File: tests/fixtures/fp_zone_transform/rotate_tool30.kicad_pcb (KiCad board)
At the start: 2 copper layers, 45 x 40 mm, 1 part

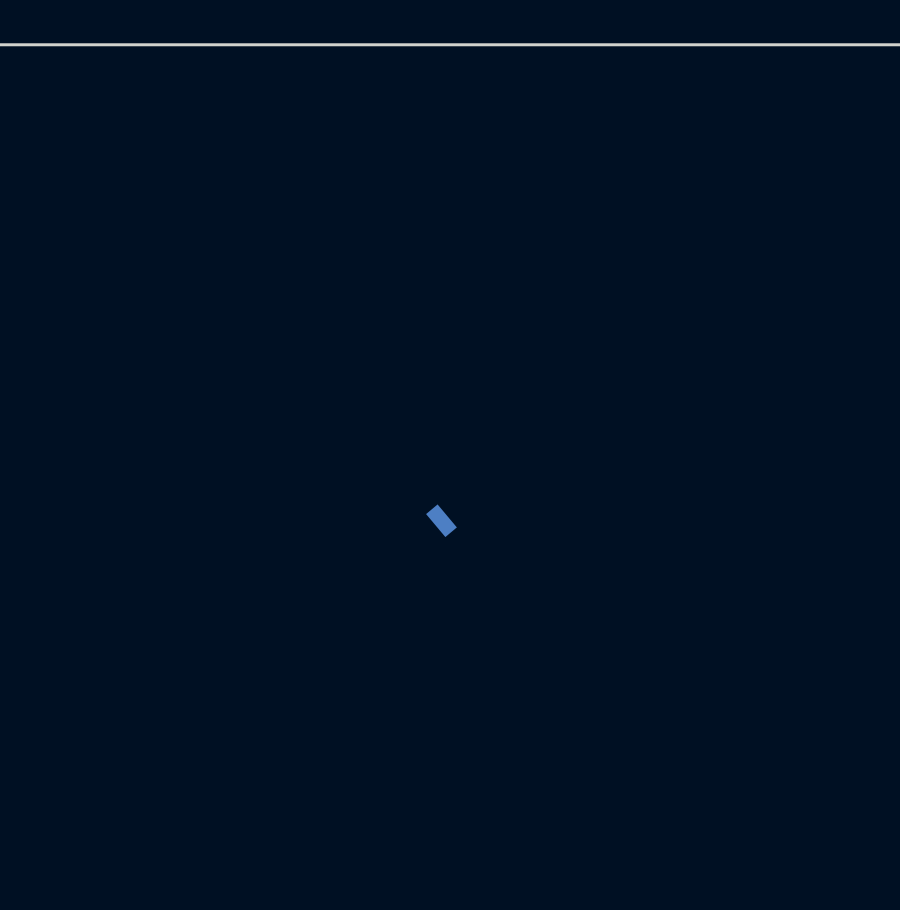
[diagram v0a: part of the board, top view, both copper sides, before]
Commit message: fix(pcb): turn footprint text angles with their footprint (#6126)
KiCad stores property/fp_text (at x y ANGLE) angles board-absolute, like
pad angles, so rotating or flipping a footprint must rewrite them. Pinned
against pcbnew 10.0.1 goldens (tests/fixtures/fp_zone_transform/, now
carrying keep-upright and unlocked user texts plus Rotate() cases):

- Footprint.__setattr__ maps text angles from the old placement frame to
  the new one (SetOrientation semantics: +delta on the same side, a -> -a
  under the left/right side swap), for both the S-expression nodes and the
  parsed FootprintText objects. This covers update_footprint_position,
  placement writeback, pcb move-footprint and snap-rotation.
- Footprint.keep_texts_upright / keep_footprint_texts_upright apply
  KiCad's FOOTPRINT::Rotate keep-upright step (>= 180 turns by -180 and
  swaps justification; (unlocked yes) / legacy `unlocked` texts are left
  alone). Used by pcb modify rotate, the recovery rotate strategy and the
  mirror strategy (pcb modify flip), replacing its `180 - a` text angle,
  which was 180 degrees off for unlocked and some keep-upright text.
- transform_footprint_text_nodes is the raw-node counterpart of
  transform_footprint_zone_nodes, used by pcb modify rotate.
- snap-rotation now turns pad angles by the snap amount.

Co-Authored-By: Claude Opus 5.5 (1M context) <noreply@anthropic.com>
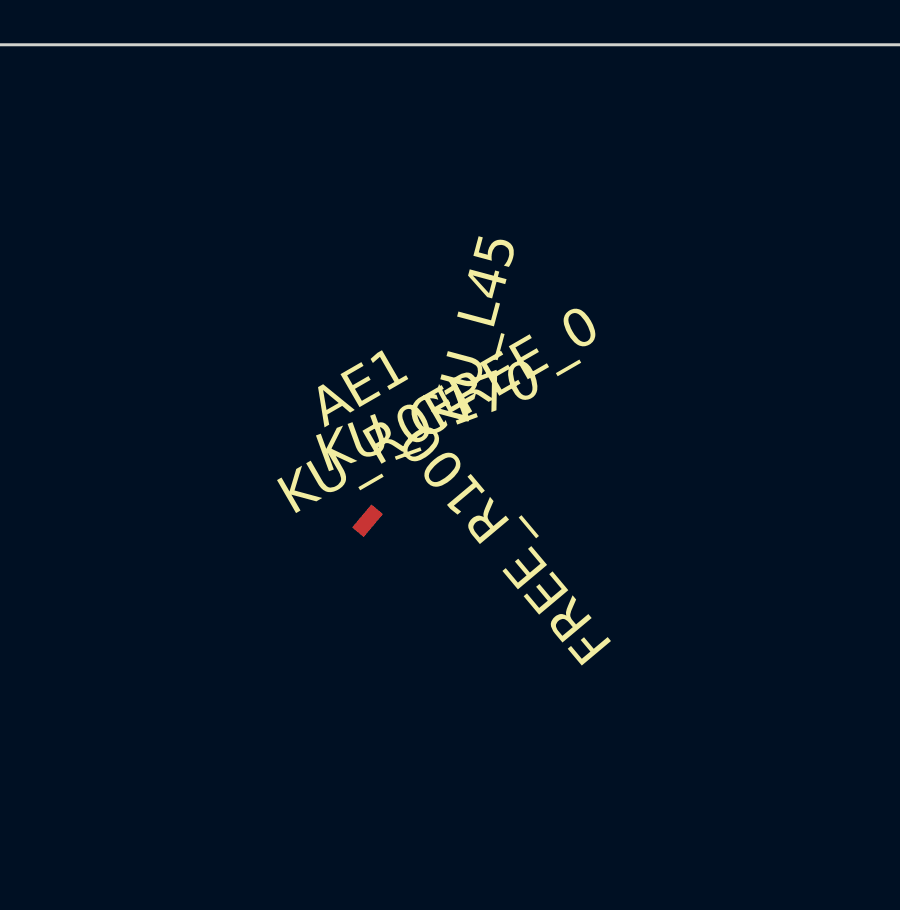
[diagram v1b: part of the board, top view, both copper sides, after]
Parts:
- AE1: moved to F.Cu
- turned AE1 to 30 degrees
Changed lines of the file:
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@@
 	)
 	(footprint ""
-		(layer "B.Cu")
-		(at 120 109 150)
+		(layer "F.Cu")
+		(at 120 109 30)
 		(property "Reference" "AE1"
-			(at 0 3 150)
-			(layer "B.SilkS")
+			(at 0 -3 30)
+			(layer "F.SilkS")
 			(effects
 				(font
 					(size 1.27 1.27)
 				)
-				(justify mirror)
 			)
 		)
 		(property "Value" "ANTENNA"
-			(at 0.5 -3 60)
-			(layer "B.Fab")
+			(at 0.5 3 120)
+			(layer "F.Fab")
 			(effects
 				(font
 					(size 1.27 1.27)
 				)
-				(justify mirror)
 			)
 		)
 		(property "Datasheet" ""
-			(at 0 0 150)
-			(layer "B.Fab")
+			(at 0 0 30)
+			(layer "F.Fab")
 			(hide yes)
 			(effects
@@
 					(size 1.27 1.27)
 				)
-				(justify mirror)
 			)
 		)
 		(property "Description" ""
-			(at 0 0 150)
-			(layer "B.Fab")
+			(at 0 0 30)
+			(layer "F.Fab")
 			(hide yes)
 			(effects
@@
 					(size 1.27 1.27)
 				)
-				(justify mirror)
 			)
 		)
 		(duplicate_pad_numbers_are_jumpers no)
-		(fp_text user "KU_L45"
-			(at 1.5 1 105)
-			(layer "B.SilkS")
+		(fp_text user "KU_C170"
+			(at 1.5 -1 20)
+			(layer "F.SilkS")
 			(effects
 				(font
 					(size 1.27 1.27)
 				)
-				(justify right bottom mirror)
 			)
 		)
-		(fp_text user "KU_R0"
-			(at 1.5 1 150)
-			(layer "B.SilkS")
+		(fp_text user "FREE_0"
+			(at 1.5 -1 30)
+			(unlocked yes)
+			(layer "F.SilkS")
 			(effects
 				(font
 					(size 1.27 1.27)
 				)
-				(justify left mirror)
+				(justify left)
 			)
 		)
-		(fp_text user "KU_C170"
-			(at 1.5 1 160)
-			(layer "B.SilkS")
+		(fp_text user "KU_R0"
+			(at 1.5 -1 30)
+			(layer "F.SilkS")
 			(effects
 				(font
 					(size 1.27 1.27)
 				)
-				(justify mirror)
+				(justify right)
 			)
 		)
-		(fp_text user "FREE_R100"
-			(at 1.5 1 230)
-			(unlocked yes)
-			(layer "B.SilkS")
+		(fp_text user "KU_L45"
+			(at 1.5 -1 75)
+			(layer "F.SilkS")
 			(effects
 				(font
 					(size 1.27 1.27)
 				)
-				(justify right bottom mirror)
+				(justify left top)
 			)
 		)
-		(fp_text user "FREE_0"
-			(at 1.5 1 330)
+		(fp_text user "FREE_R100"
+			(at 1.5 -1 130)
 			(unlocked yes)
-			(layer "B.SilkS")
+			(layer "F.SilkS")
 			(effects
 				(font
 					(size 1.27 1.27)
 				)
-				(justify left mirror)
+				(justify right bottom)
 			)
 		)
 		(pad "1" smd rect
-			(at -2 -1 130)
+			(at -2 1 50)
 			(size 1 0.5)
-			(layers "B.Cu" "B.Mask" "B.Paste")
+			(layers "F.Cu" "F.Mask" "F.Paste")
 			(thermal_bridge_angle 45)
 		)
 		(zone
-			(layer "B.Cu")
+			(layer "F.Cu")
 			(name "FP_POUR")
 			(hatch edge 0.5)
@@
 			)
 			(min_thickness 0.25)
-			(fill
+			(fill yes
 				(thermal_gap 0.5)
 				(thermal_bridge_width 0.5)
@@
 			(polygon
 				(pts
-					(xy 118.633975 109.366025) (xy 116.035898 107.866025) (xy 114.535898 110.464102) (xy 117.633975 111.098076)
+					(xy 121.366025 109.366025) (xy 123.964102 107.866025) (xy 125.464102 110.464102) (xy 122.366025 111.098076)
 				)
 			)
 		)
 		(zone
-			(layer "B.Cu")
+			(layer "F.Cu")
 			(name "ANT_KEEPOUT")
 			(hatch edge 0.5)
@@
 			(polygon
 				(pts
-					(xy 124.598076 107.035898) (xy 119.401924 104.035898) (xy 117.901924 106.633975) (xy 119.866025 111.232051)
-					(xy 121.598076 112.232051)
+					(xy 115.401924 107.035898) (xy 120.598076 104.035898) (xy 122.098076 106.633975) (xy 120.133975 111.232051)
+					(xy 118.401924 112.232051)
 				)
 			)
